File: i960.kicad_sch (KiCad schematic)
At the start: 60 parts

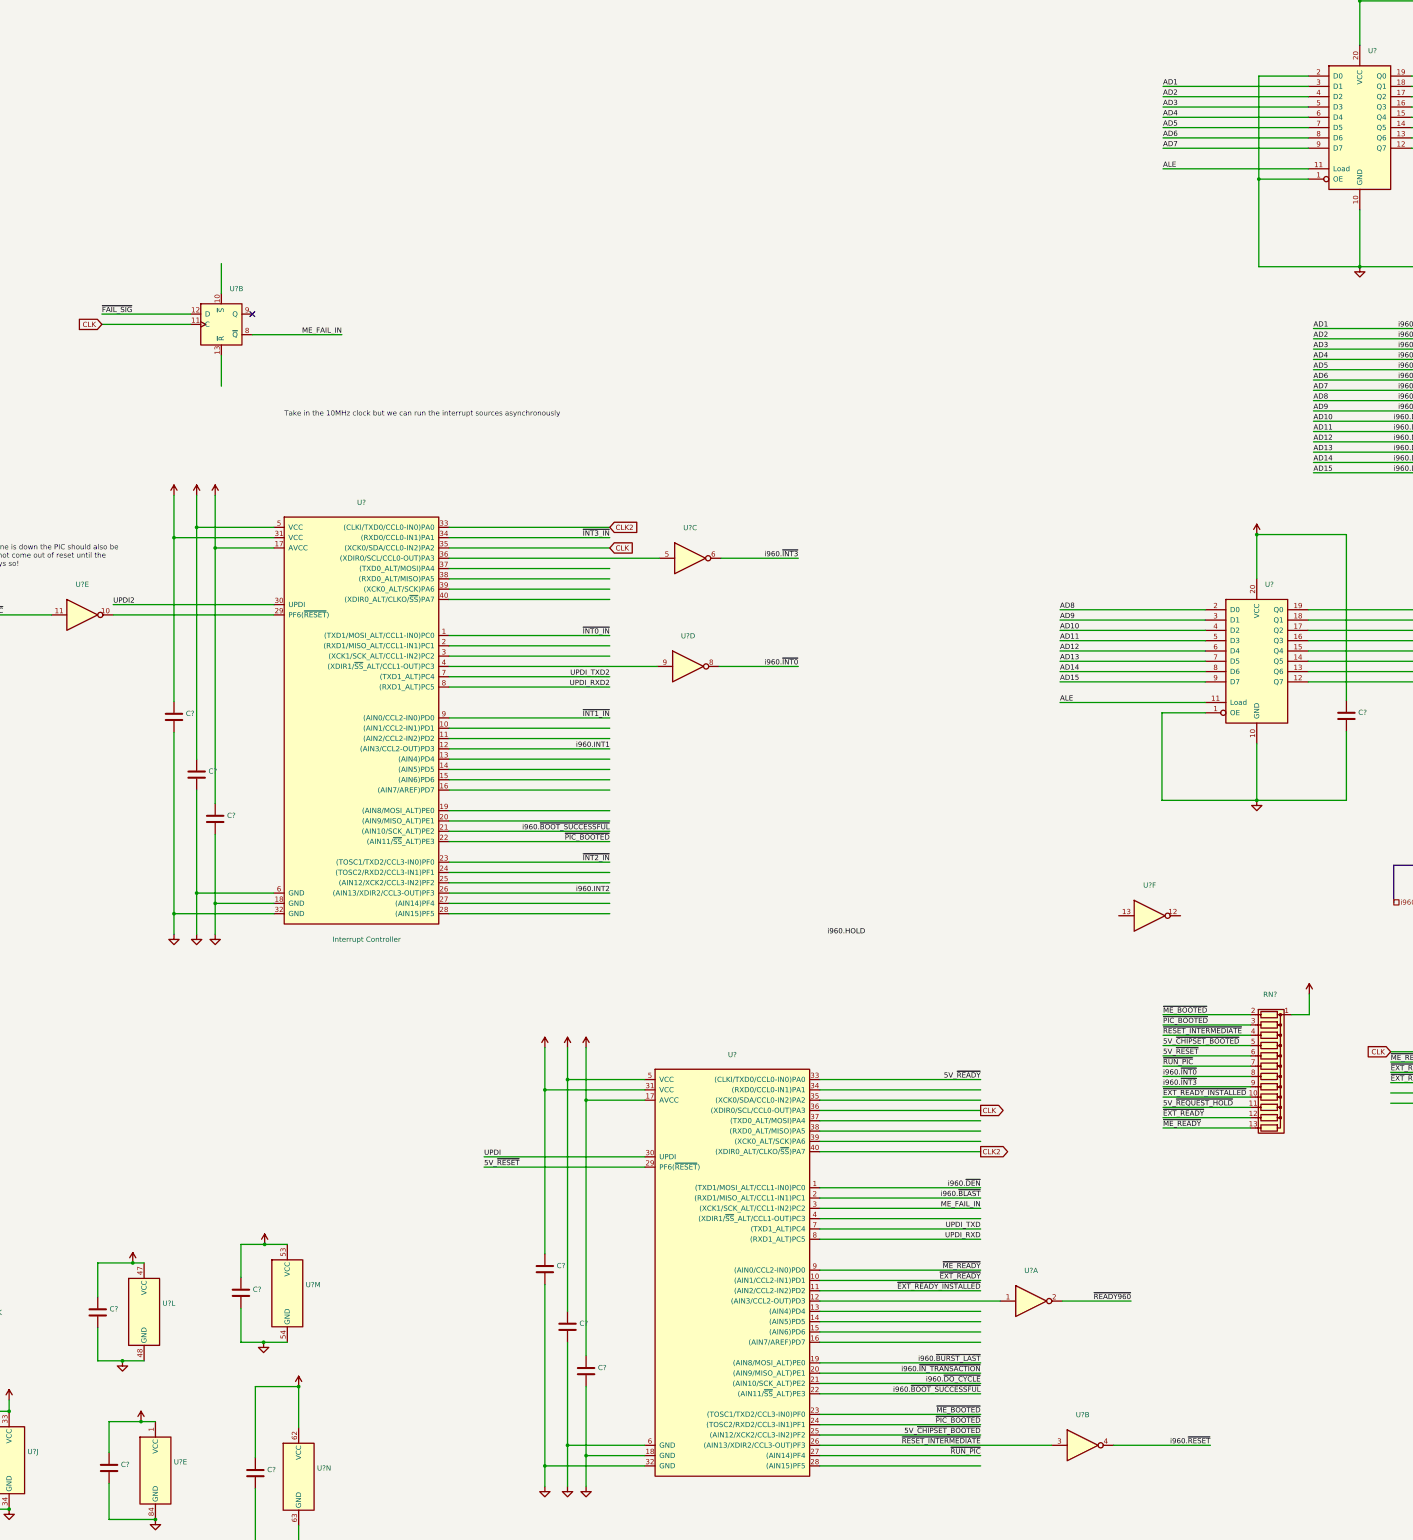
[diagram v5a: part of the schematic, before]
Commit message: Use an AHC174 to handle teh fail sync
I realized that we can just pass the sync'd result without doing an
invert at all. It means that I can easily resolve the logic in the
management engine without shenanigans!

I am also thinking that it provides a better ready signal sync backup
than the external device. I can just reroute it easily
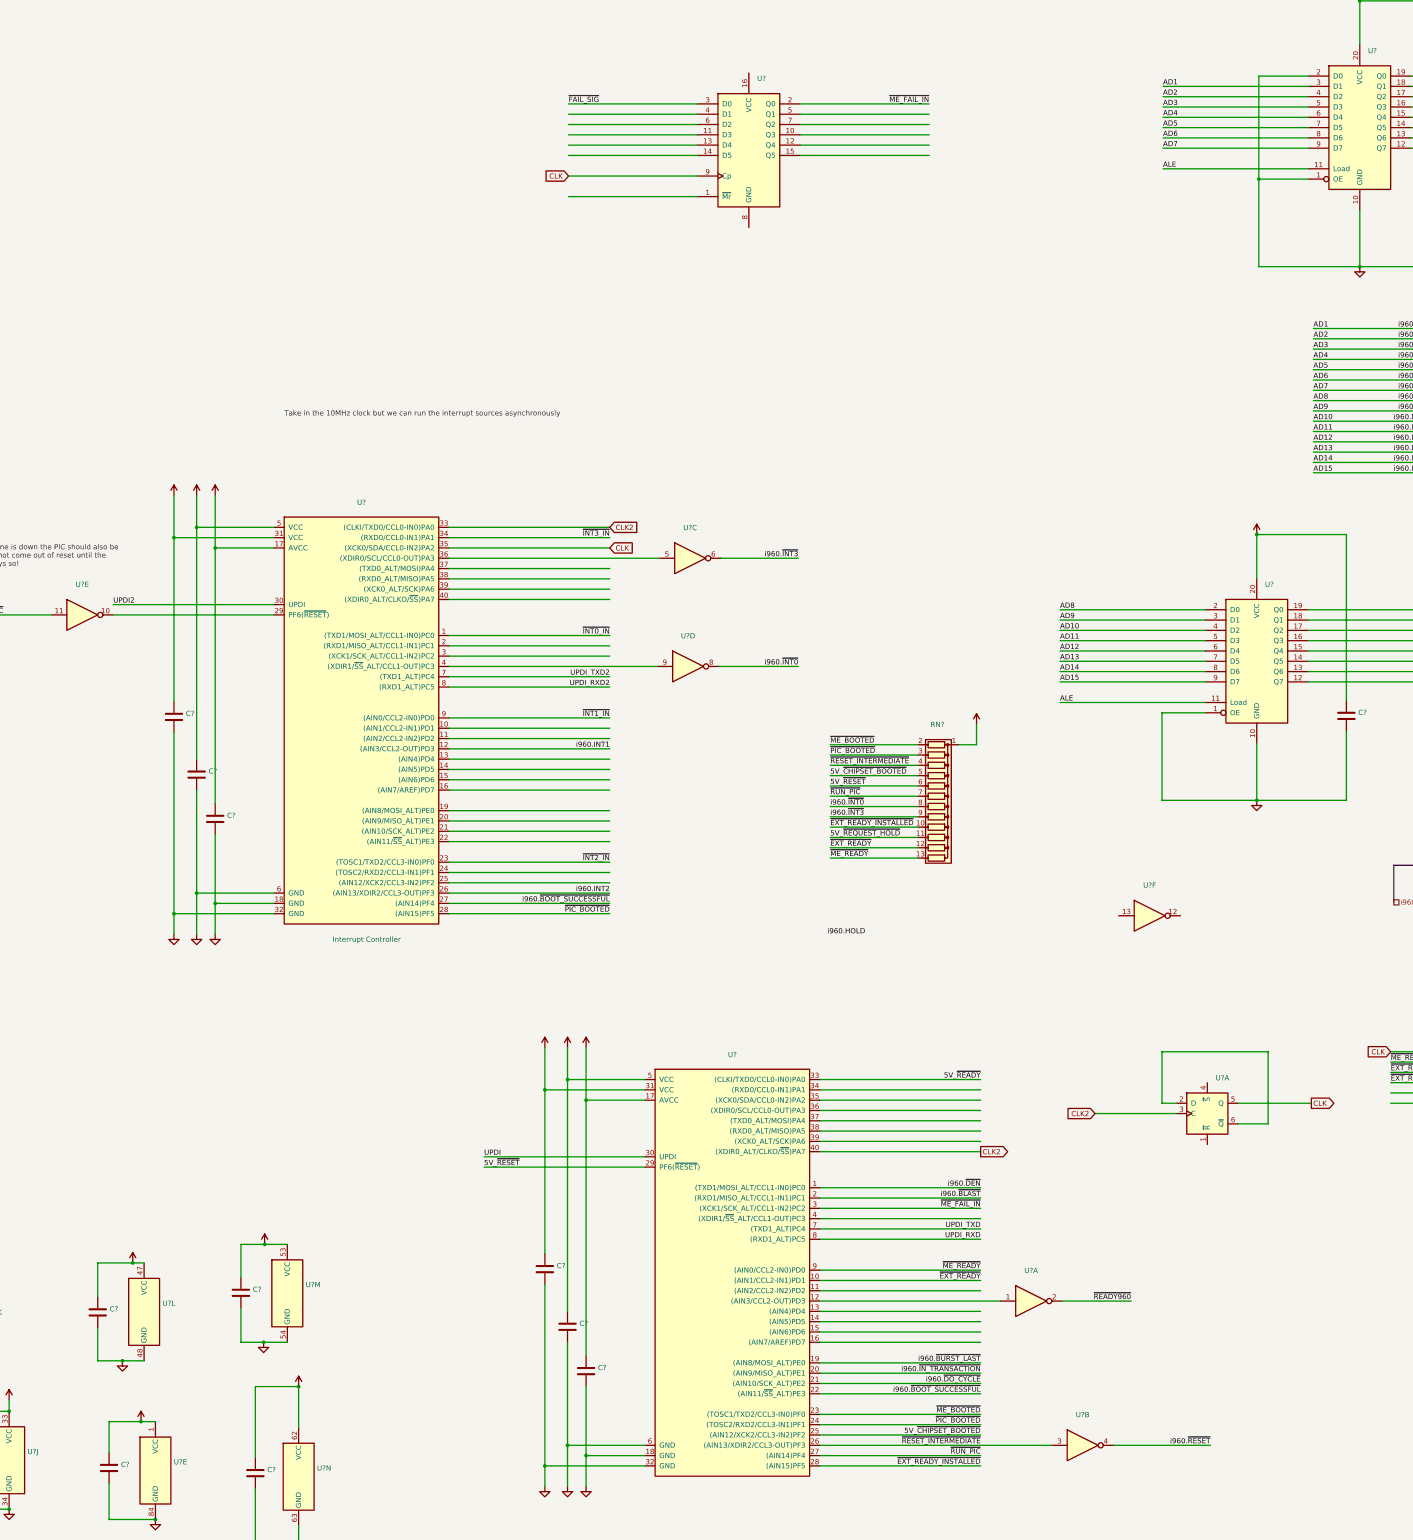
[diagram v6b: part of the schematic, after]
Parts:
- removed U?: (no value), symbol 74xx:74HC74
- added U?: (no value), symbol 74xx:74HC74
- added U?: (no value), symbol 74xx:74LS174
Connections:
- net CLK: now also U?.5 (Q), U?.9 (Cp); no longer U?.36 ((XDIR0/SCL/CCL0-OUT)PA3)
- net CLK2: now also U?.3 (C)
- net i960.~{BOOT_SUCCESSFUL}: now also U?.27 ((AIN14)PF4); no longer U?.21 ((AIN10/SCK_ALT)PE2)
- net ~{EXT_READY_INSTALLED}: now also U?.28 ((AIN15)PF5); no longer U?.11 ((AIN2/CCL2-IN2)PD2)
- net ~{FAIL_SIG}: now also U?.3 (D0)
- net ~{PIC_BOOTED}: now also U?.28 ((AIN15)PF5); no longer U?.22 ((AIN11/~{SS}_ALT)PE3)
- net ME_FAIL_IN renamed ~{ME_FAIL_IN}
- net ~{ME_FAIL_IN}: now also U?.2 (Q0)
- new net: U?.2 (D), U?.6 (~{Q})
- no-connect marks 1 -> 0
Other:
- moved on the sheet: RN?

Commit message: Just connect HOLD directly to the i960 through an inverter from GCM4
No need for extra logic because the hold will handle that
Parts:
- removed J?: (no value), symbol Connector_Generic:Conn_01x08
- removed U?: (no value), symbol 74xx:74HC74
- added C? (x2): (no value), symbol Device:C
- added U? (x3): (no value), symbol 74xx:74HC00
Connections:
- net +5V: now also U?.16 (VCC), C?.1, C?.1, U?.14 (VCC)
- net 5V_~{REQUEST_HOLD}: no longer U?.9 (2Y3)
- net CLK: now also U?.36 ((XDIR0/SCL/CCL0-OUT)PA3)
- net GND: now also U?.8 (GND), C?.2, C?.2, U?.7 (GND)
- net i960.HOLD: now also U?.12
- net ~{EXT_READY_INSTALLED}: no longer U?.28 ((AIN15)PF5)
- net ~{EXT_READY}: now also U?.11; no longer RN?.12 (R11)
- net ~{ME_READY}: now also U?.4 (D1)
- net ~{HOLD}: now reaches U?.13
- net ~{MR}: now reaches U?.1 (~{Mr})
- net ~{MR}: now also RN?.12 (R11)
- net ~{RDY_P0}: now reaches U?.5 (Q1)
- net ~{RDY_P0}: now also U?.6 (D2), U?.1, U?.2
- net ~{RDY_P1}: now reaches U?.7 (Q2)
- net ~{RDY_P1}: now also U?.12
- net ~{REQUEST_HOLD}: no longer names the net of U?.11 (2A3)
- new net: U?.13, U?.3
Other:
- moved on the sheet: U?A, U?F

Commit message: Use an inverter and and-gate combo with the hex flip flop
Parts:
- removed C? (x2): (no value), symbol Device:C
- removed U? (x3): (no value), symbol 74xx:74HC00
- removed U? (x2): (no value), symbol 74xx:74HC74
- removed U?: (no value), symbol 74xx:74AHC04
- added U? (x2): (no value), symbol 74xx:74LS08
- added U?: (no value), symbol 74xx:74AHC04
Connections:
- net 5V_~{REQUEST_HOLD} is gone; now on net ~{MR}: RN?.11 (R10)
- net +5V: now also U?.14 (VCC)
- net GND: now also U?.7 (GND)
- net ~{ME_READY}: now also RN?.12 (R11); no longer RN?.13 (R12)
- net ~{MR}: no longer RN?.12 (R11)
- net ~{RDY_P0}: now also U?.13
- net ~{RDY_P1}: now also U?.2
- net ~{EXT_READY} renamed EXT_READY
- net EXT_READY: now also U?.3
- new net: U?.1, U?.12
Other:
- note removed: "Take in the 10MHz clock but we can run the interrupt sources asynchronously"
- moved on the sheet: C?, U?, U?G
